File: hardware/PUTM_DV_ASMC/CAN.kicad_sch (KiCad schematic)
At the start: 0 parts

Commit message: can section
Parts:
- added C10, C23, C25, C9: 100n, Capacitor_SMD:C_0603_1608Metric_Pad1.08x0.95mm_HandSolder, symbol Device:C_Small
- added C11, C12, C24, C28: 10n, Capacitor_SMD:C_0603_1608Metric_Pad1.08x0.95mm_HandSolder, symbol Device:C_Small
- added C13, C15, C17, C18, C19, C20, C21, C22: 47u, Capacitor_SMD:C_0805_2012Metric_Pad1.18x1.45mm_HandSolder, symbol Device:C_Small
- added C14, C16: 4.7nF/Y2, Samacsys:CAPC5728X280N, symbol Samacsys_kicad_sym:S252B222K502CT
- added FB1, FB2, FB3, FB4, FB5, FB6, FB7, FB8: 2K@100MHz, Inductor_SMD:L_0805_2012Metric_Pad1.05x1.20mm_HandSolder, symbol Device:FerriteBead_Small
- added R1, R2: 100K, Resistor_SMD:R_0603_1608Metric_Pad0.98x0.95mm_HandSolder, symbol Device:R_Small
- added U1, U2: ADM3057ExRW, Package_SO:SOIC-20W_7.5x12.8mm_P1.27mm, symbol Interface_CAN_LIN:ADM3057ExRW
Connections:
- new net: C20.2, FB6.1, U2.3 (VCC)
- new net: C17.1, FB2.2, U1.18 (GNDISO), U1.20 (GNDISO)
- new net: C22.2, FB5.1, U1.3 (VCC)
- new net: R2.2, U2.12 (RS)
- new net: C10.2, C12.1, C15.2, FB3.1, U2.16 (VISOIN)
- new net: C18.1, FB4.2, U2.18 (GNDISO), U2.20 (GNDISO)
- new net: C18.2, FB3.2, U2.19 (VISOOUT)
- new net: C24.1, FB8.1, U2.4 (VIO)
- new net: R1.2, U1.12 (RS)
- new net: C11.1, C13.2, C9.2, FB1.1, U1.16 (VISOIN)
- new net: C17.2, FB1.2, U1.19 (VISOOUT)
- new net: C28.1, FB7.1, U1.4 (VIO)
- new net +3.3V: C23.1, C25.1, FB7.2, FB8.2
- new net +5V: C19.2, C21.2, FB5.2, FB6.2
- new net CAN1+: U1.14 (CANH)
- new net CAN1-: U1.13 (CANL)
- new net CAN1_RX: U1.5 (RXD)
- new net CAN1_TX: U1.7 (TXD)
- new net CAN2+: U2.14 (CANH)
- new net CAN2-: U2.13 (CANL)
- new net CAN2_RX: U2.5 (RXD)
- new net CAN2_TX: U2.7 (TXD)
- new net GND: C14.1, C16.1, C19.1, C20.1, C21.1, C22.1, C23.2, C24.2, C25.2, C28.2, U1.1 (GND1), U1.10 (GND1), U1.2 (GND1), U1.9 (AUXIN), U2.1 (GND1), U2.10 (GND1), U2.2 (GND1), U2.9 (AUXIN)
- new net GND_CAN_ISO1: C11.2, C13.1, C14.2, C9.1, FB2.1, R1.1, U1.11 (GND2), U1.15 (GND2)
- new net GND_CAN_ISO2: C10.1, C12.2, C15.1, C16.2, FB4.1, R2.1, U2.11 (GND2), U2.15 (GND2)
- new net STBY_CAN_1: U1.8 (STBY)
- new net STBY_CAN_2: U2.8 (STBY)
- no-connect marks 0 -> 4
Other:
- note added: "1*"
- note added: "1* Slope control for 5 Mbps"
- title: (none) -> CAN communication section

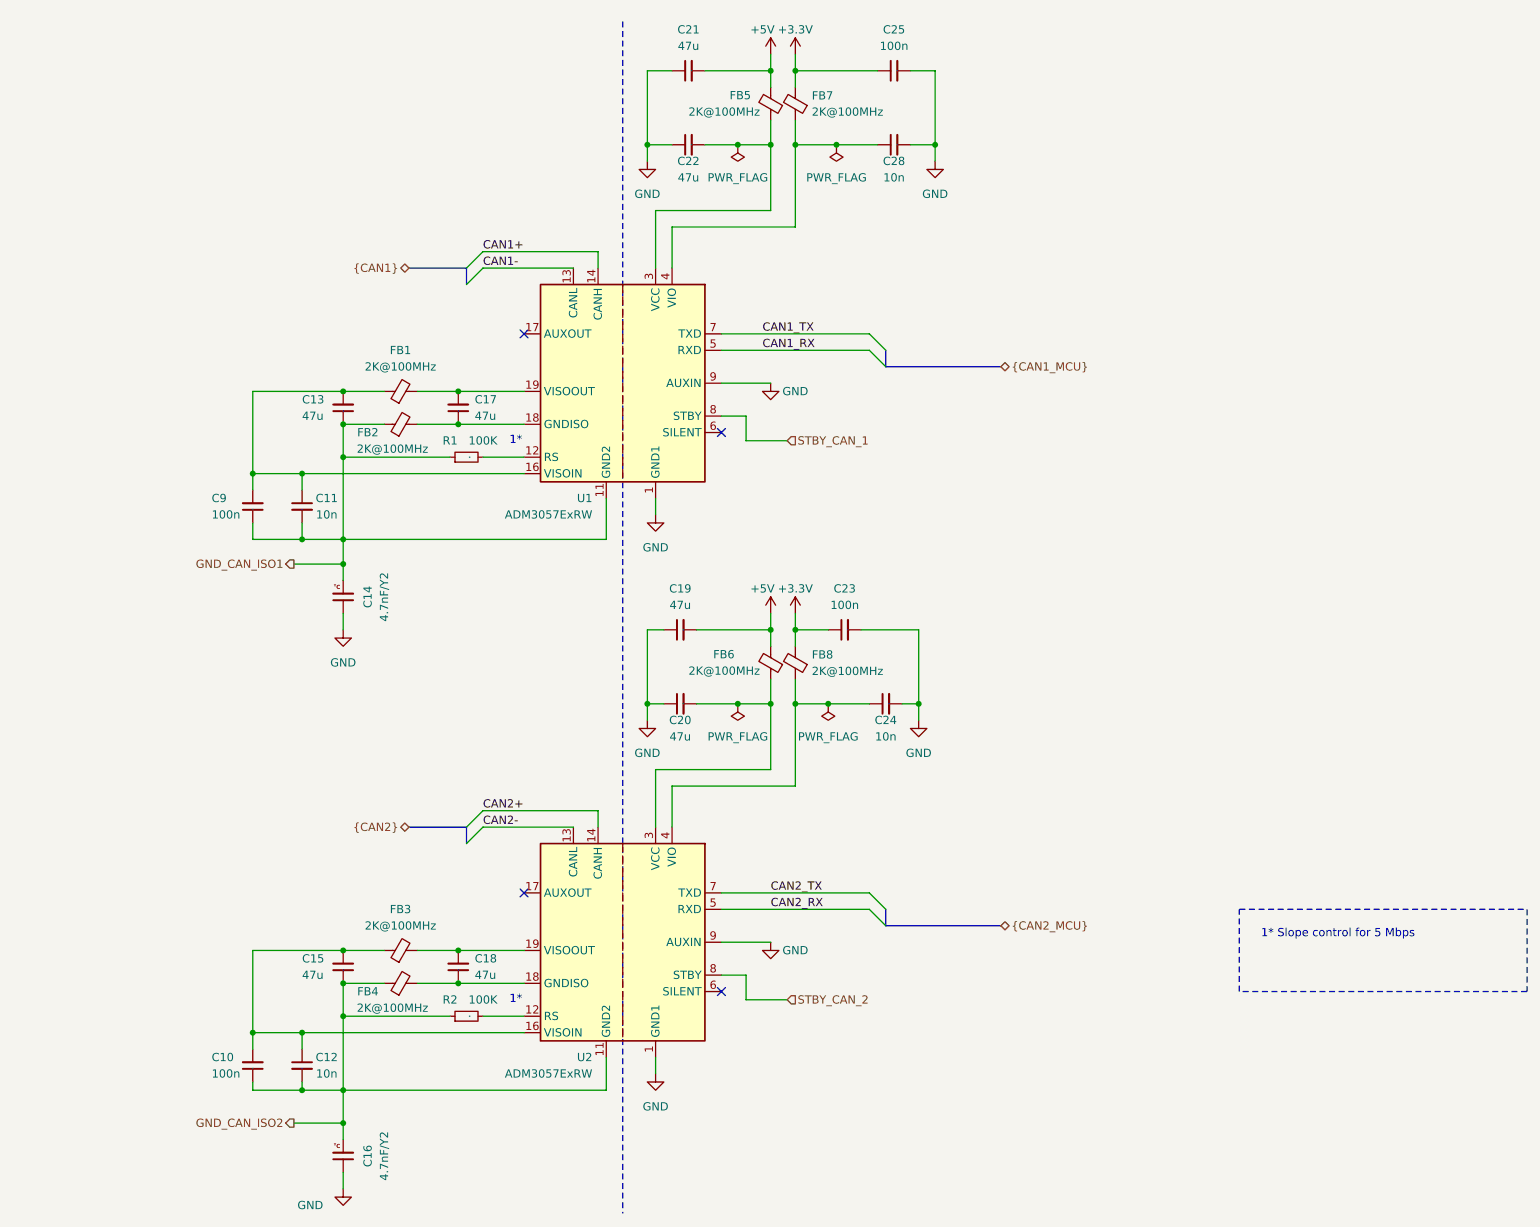
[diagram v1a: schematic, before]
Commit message: schematics without main connector
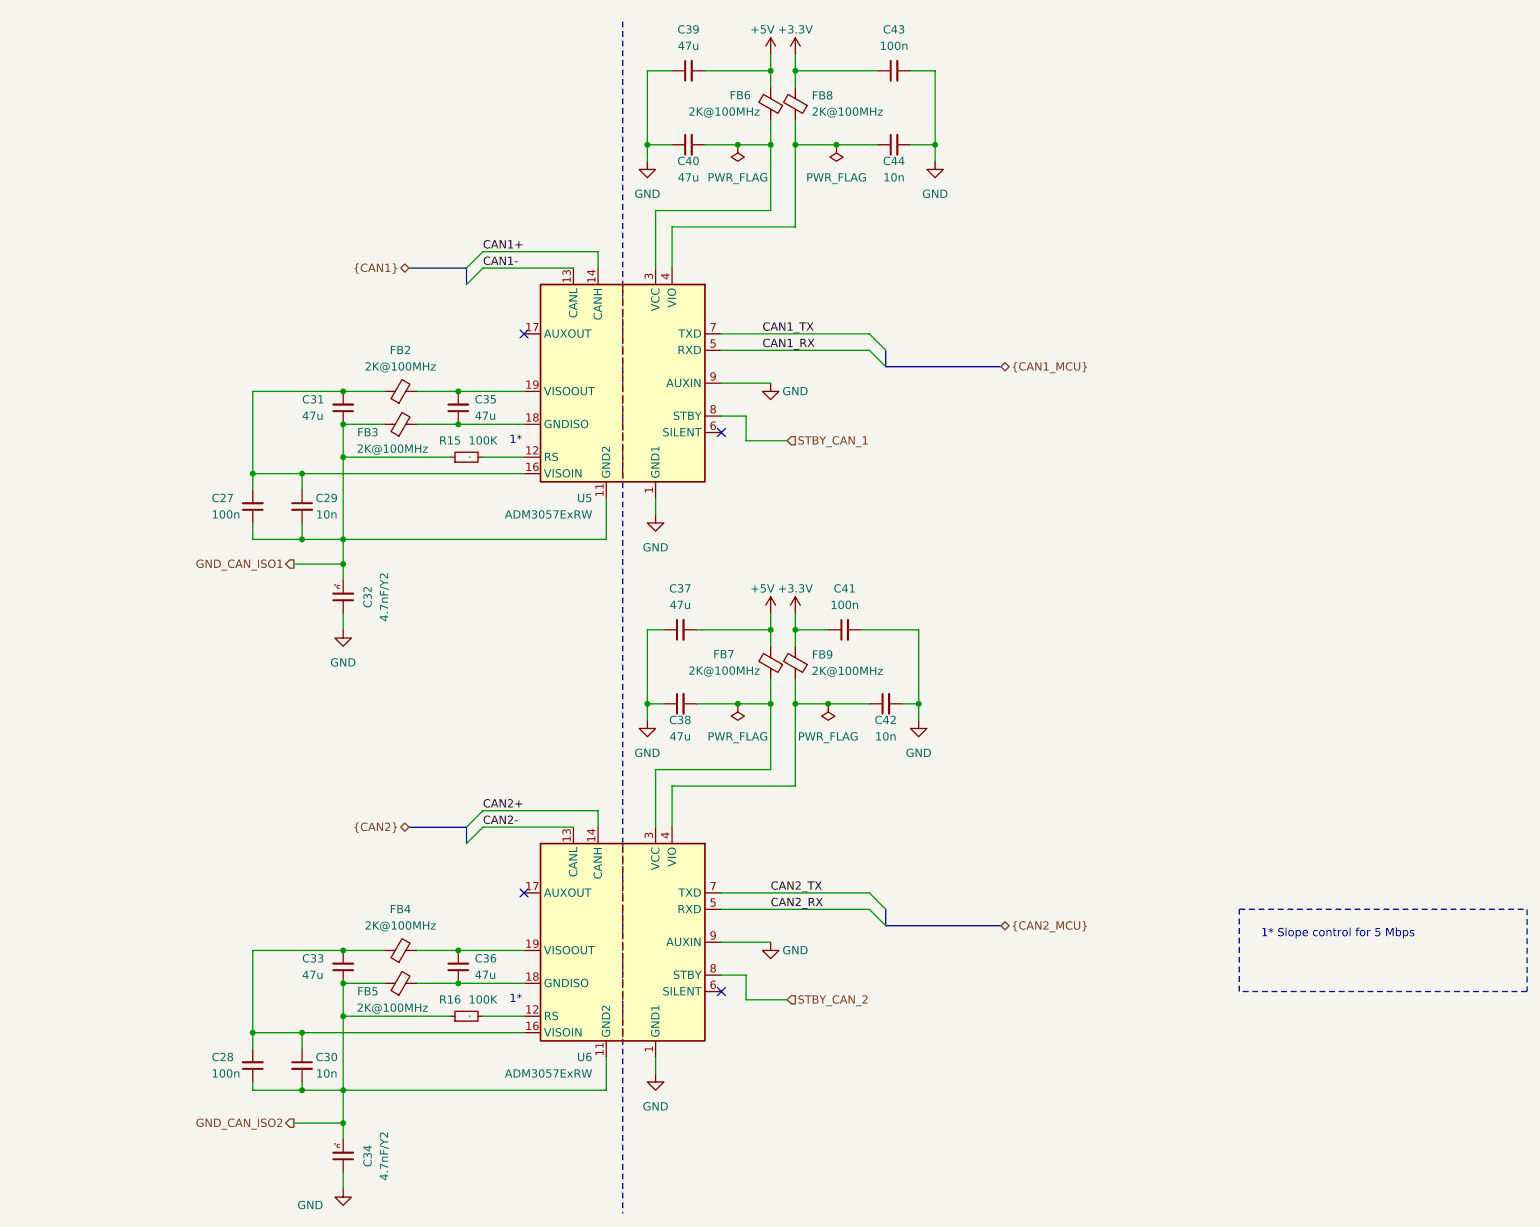
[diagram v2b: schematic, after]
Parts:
- renumbered C9 to C27, C10 to C28, C11 to C29, C12 to C30, C13 to C31, C14 to C32, C15 to C33, C16 to C34, C17 to C35, C18 to C36, C19 to C37, C20 to C38, C21 to C39, C22 to C40, C23 to C41, C24 to C42, C25 to C43, C28 to C44, FB1 to FB2, FB2 to FB3, FB3 to FB4, FB4 to FB5, FB5 to FB6, FB6 to FB7, FB7 to FB8, FB8 to FB9, R1 to R15, R2 to R16, U1 to U5, U2 to U6

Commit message: schematic without error
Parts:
- C32, C34: footprint Samacsys:CAPC5728X280N -> CAPC5728X280N:CAPC5728X280N
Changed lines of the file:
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@@
 			)
 		)
-		(property "Footprint" "Samacsys:CAPC5728X280N"
+		(property "Footprint" "CAPC5728X280N:CAPC5728X280N"
 			(at 195.25 180.34 0)
 			(hide yes)
@@
 			)
 		)
-		(property "Footprint" "Samacsys:CAPC5728X280N"
+		(property "Footprint" "CAPC5728X280N:CAPC5728X280N"
 			(at 195.25 93.98 0)
 			(hide yes)

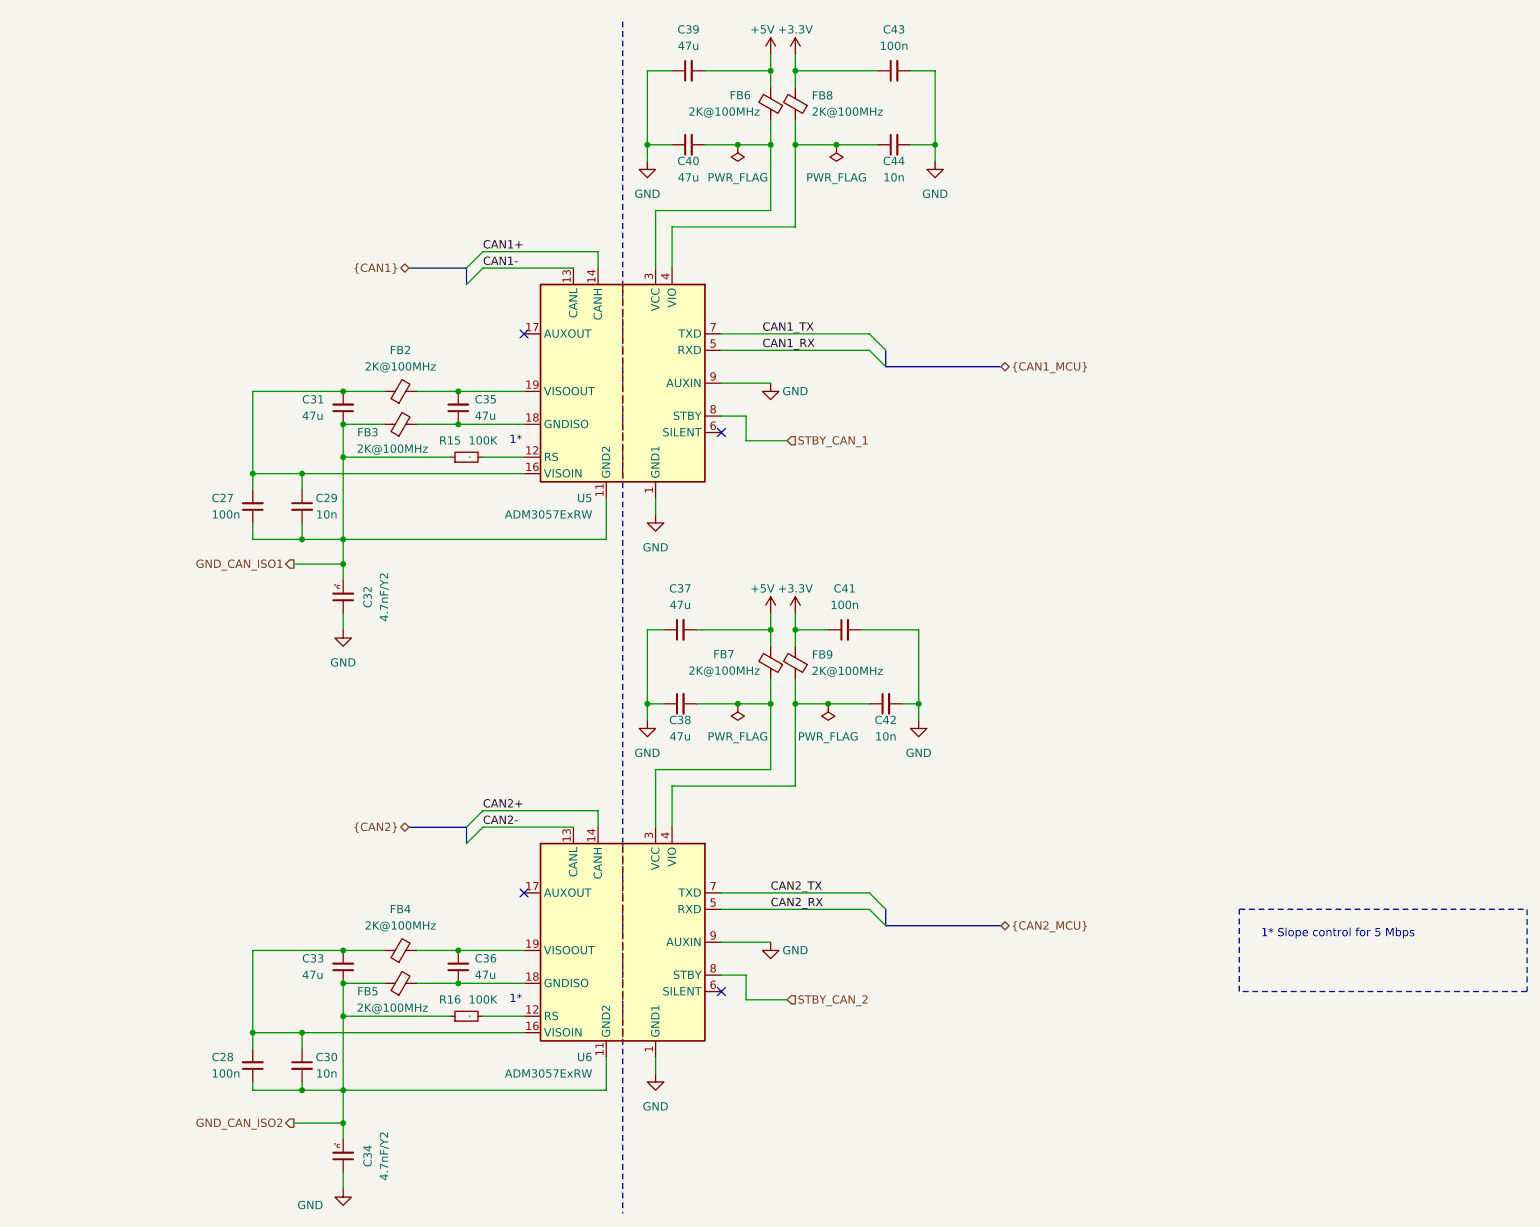
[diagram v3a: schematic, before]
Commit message: tylko dwa bledy z can - schemat na wykonczeniu
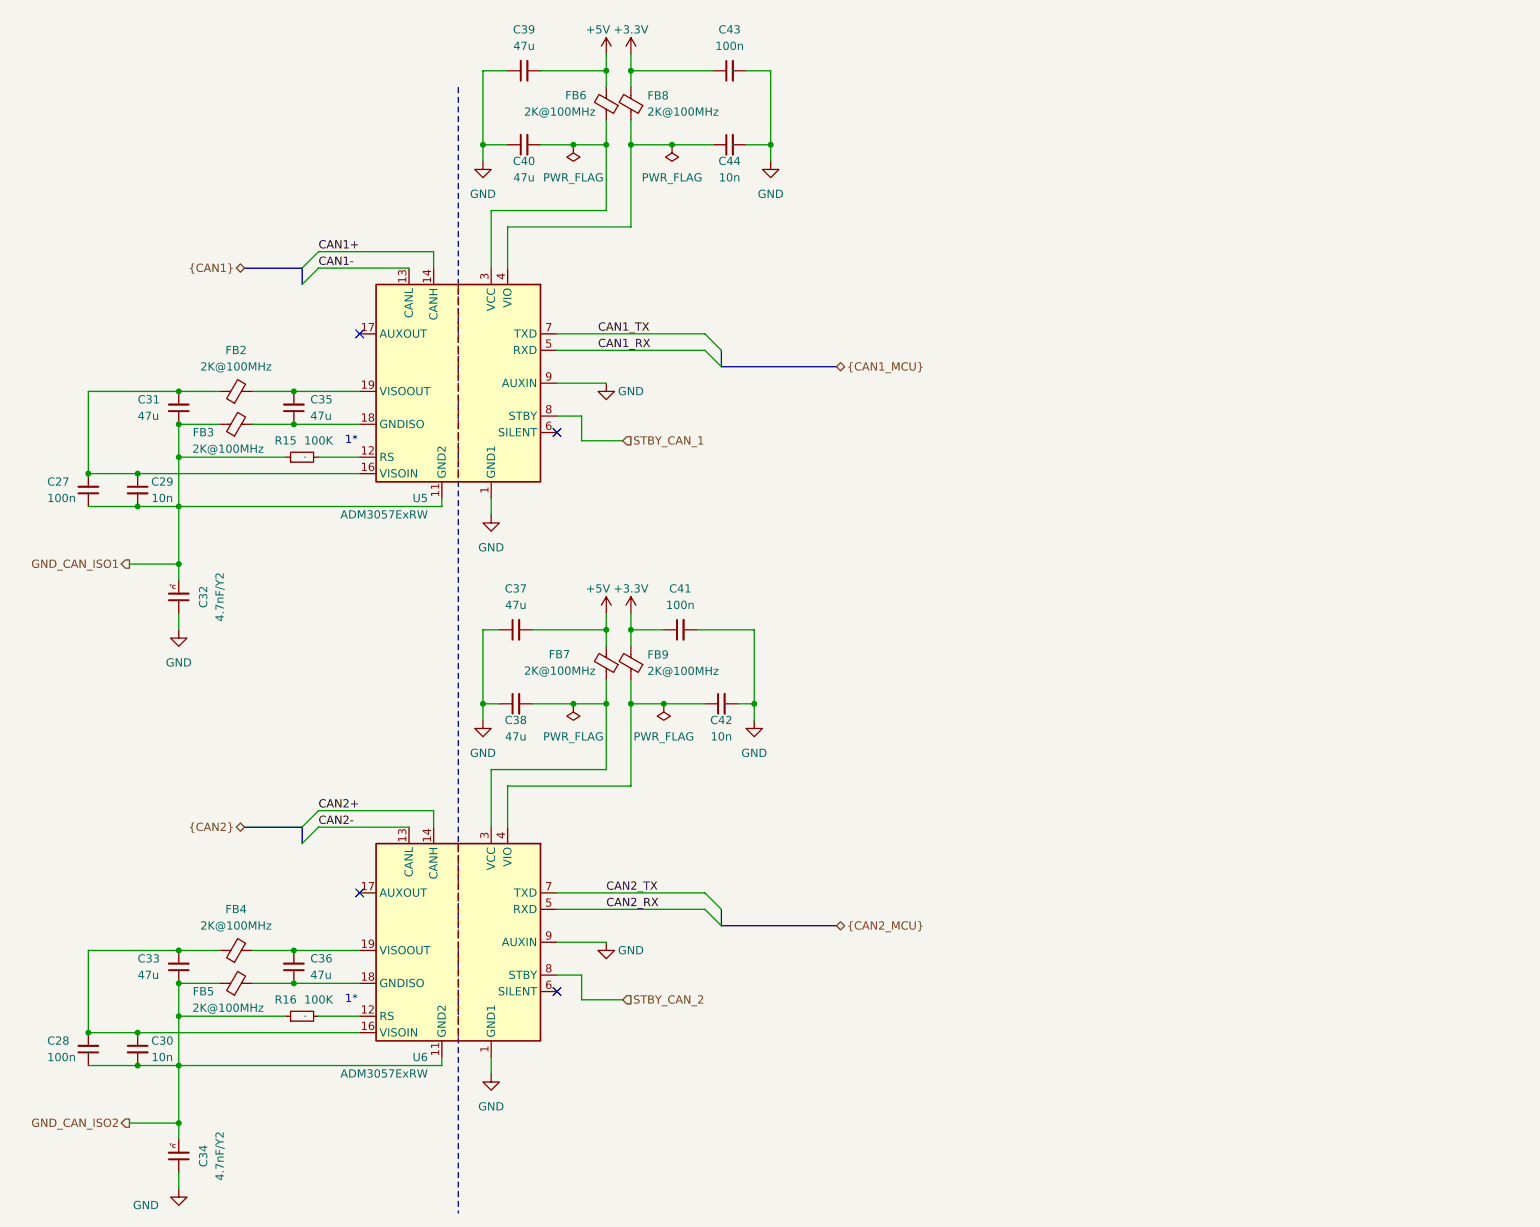
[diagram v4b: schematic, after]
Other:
- note removed: "1* Slope control for 5 Mbps"

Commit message: work on supply and zones
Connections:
- net +3.3V renamed +3V3

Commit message: work work work
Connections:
- net CAN1+ renamed CAN1_P
- net CAN1- renamed CAN1_N
- net CAN2+ renamed CAN2_P
- net CAN2- renamed CAN2_N
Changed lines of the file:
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@@
 		)
 	)
-	(label "CAN1-"
+	(label "CAN1_N"
 		(at 95.25 52.07 0)
+		(effects
+			(font
+				(size 1.27 1.27)
+			)
+			(justify left bottom)
+		)
+	)
+	(label "CAN1_RX"
+		(at 138.43 64.77 0)
+		(effects
+			(font
+				(size 1.27 1.27)
+			)
+			(justify left bottom)
+		)
+	)
+	(label "CAN2_N"
+		(at 95.25 138.43 0)
+		(effects
+			(font
+				(size 1.27 1.27)
+			)
+			(justify left bottom)
+		)
+	)
+	(label "CAN1_TX"
+		(at 138.43 62.23 0)
 		(effects
 			(font
@@
 		)
 	)
-	(label "CAN1_RX"
-		(at 138.43 64.77 0)
+	(label "CAN1_P"
+		(at 95.25 49.53 0)
 		(effects
 			(font
@@
 		)
 	)
-	(label "CAN2-"
-		(at 95.25 138.43 0)
+	(label "CAN2_P"
+		(at 95.25 135.89 0)
 		(effects
 			(font
@@
 		)
 	)
-	(label "CAN1_TX"
-		(at 138.43 62.23 0)
-		(effects
-			(font
-				(size 1.27 1.27)
-			)
-			(justify left bottom)
-		)
-	)
-	(label "CAN1+"
-		(at 95.25 49.53 0)
-		(effects
-			(font
-				(size 1.27 1.27)
-			)
-			(justify left bottom)
-		)
-	)
-	(label "CAN2+"
-		(at 95.25 135.89 0)
-		(effects
-			(font
-				(size 1.27 1.27)
-			)
-			(justify left bottom)
-		)
-	)
 	(hierarchical_label "STBY_CAN_1"
 		(shape input)
 		(at 142.24 78.74 0)
-		(effects
-			(font
-				(size 1.27 1.27)
-			)
-			(justify left)
-		)
-	)
-	(hierarchical_label "{CAN1_MCU}"
-		(shape bidirectional)
-		(at 175.26 67.31 0)
-		(effects
-			(font
-				(size 1.27 1.27)
-			)
-			(justify left)
-		)
-	)
-	(hierarchical_label "STBY_CAN_2"
-		(shape input)
-		(at 142.24 165.1 0)
 		(effects
 			(font
@@
 		)
 	)
+	(hierarchical_label "STBY_CAN_2"
+		(shape input)
+		(at 142.24 165.1 0)
+		(effects
+			(font
+				(size 1.27 1.27)
+			)
+			(justify left)
+		)
+	)
+	(hierarchical_label "{CAN1_MCU}"
+		(shape bidirectional)
+		(at 175.26 67.31 0)
+		(effects
+			(font
+				(size 1.27 1.27)
+			)
+			(justify left)
+		)
+	)

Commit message: update pcb after review
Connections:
- net CAN1_RX renamed CAN1-
- net CAN1_TX renamed CAN1+
- net CAN2_RX renamed CAN2-
- net CAN2_TX renamed CAN2+
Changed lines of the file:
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@@
 		)
 	)
-	(label "CAN1_RX"
+	(label "CAN1-"
 		(at 138.43 64.77 0)
 		(effects
@@
 		)
 	)
-	(label "CAN1_TX"
+	(label "CAN1+"
 		(at 138.43 62.23 0)
 		(effects
@@
 		)
 	)
-	(label "CAN2_TX"
+	(label "CAN2+"
 		(at 139.7 148.59 0)
 		(effects
@@
 		)
 	)
-	(label "CAN2_RX"
+	(label "CAN2-"
 		(at 139.7 151.13 0)
 		(effects
